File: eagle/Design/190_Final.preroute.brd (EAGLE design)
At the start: 160 x 100 mm, 29 parts, among them U1_0_BRAIN ADAFRUIT-PRO-TRINKET-5V-BOB, U1_6_CASTER CASTERADAFRUIT-3/4IN, U1_7_CASTER_2 CASTERADAFRUIT-3/4IN

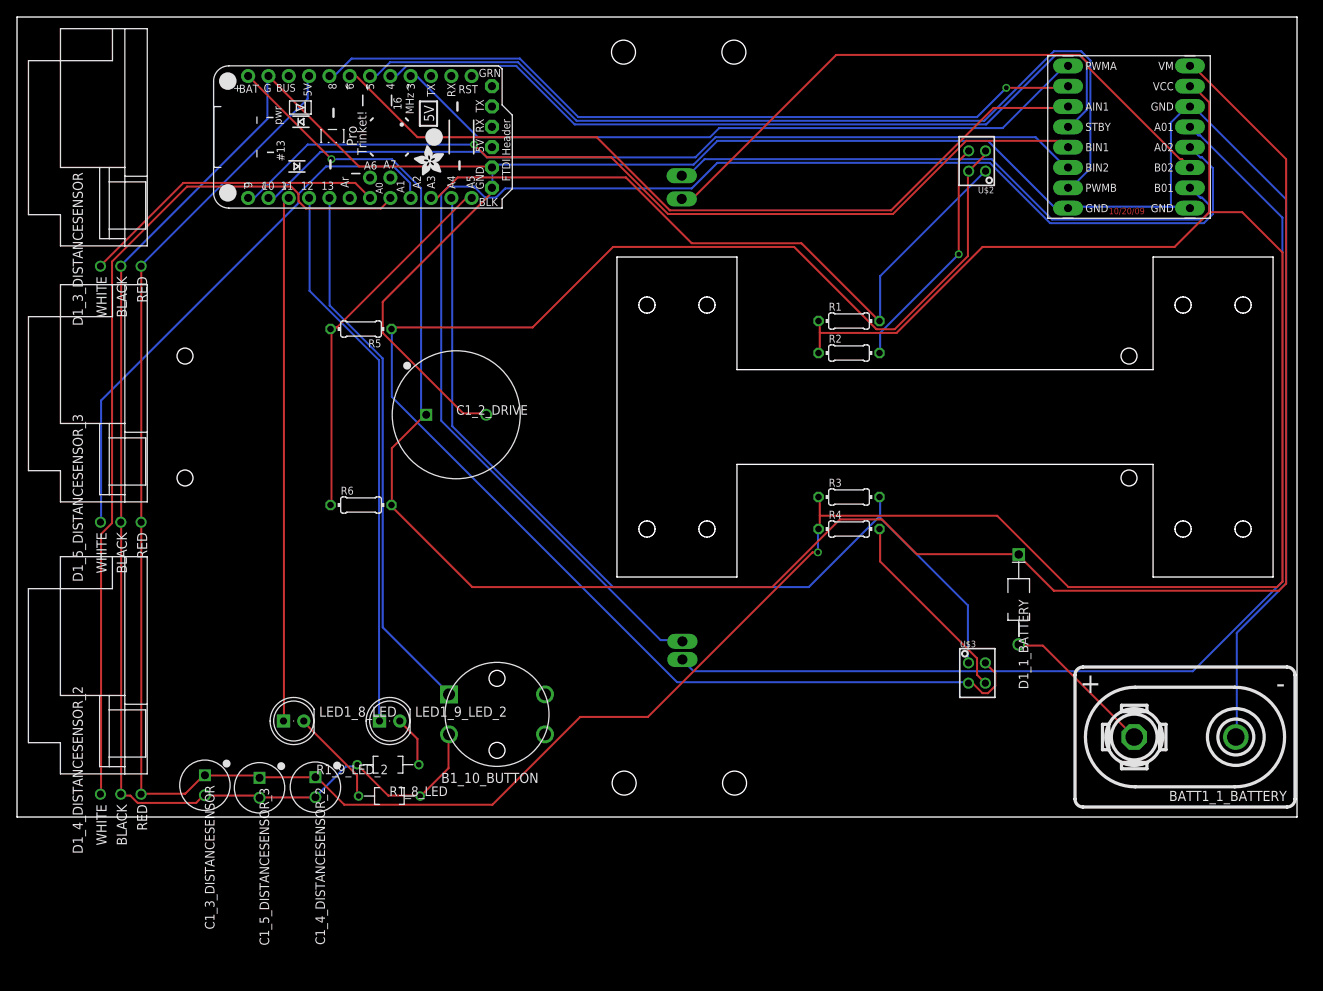
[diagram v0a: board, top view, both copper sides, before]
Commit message: caught a nasty electric bug
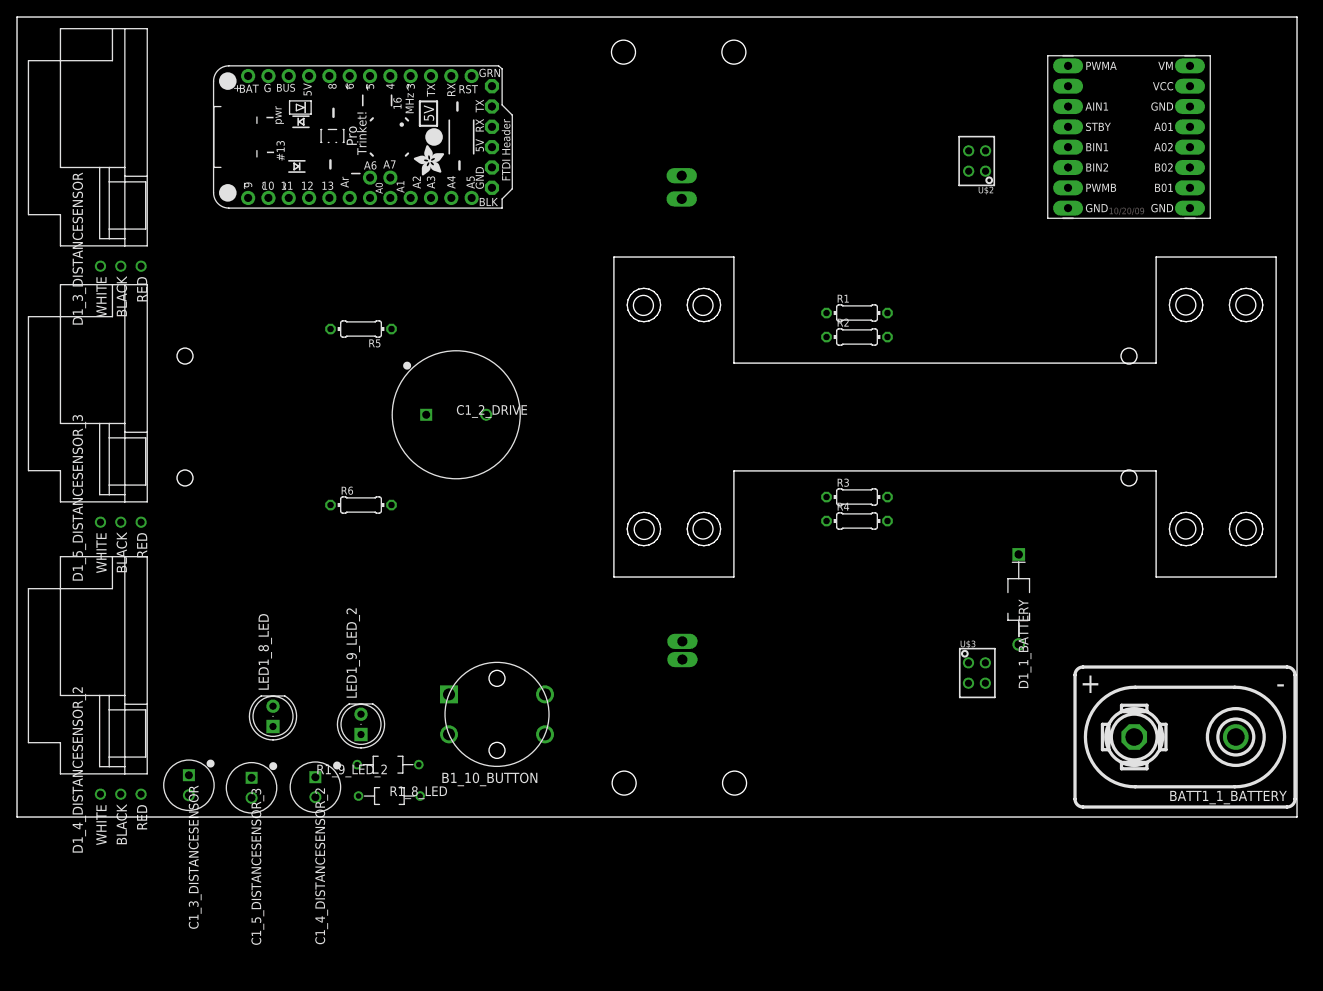
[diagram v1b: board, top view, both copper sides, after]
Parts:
- moved LED1_9_LED_2 3.60 mm to (-37.0, -38.4), turned to 90 degrees
- moved LED1_8_LED 2.64 mm to (-48.0, -37.4), turned to 90 degrees
- moved R2 2.24 mm to (25.0, 10.0)
- moved C1_3_DISTANCESENSOR 2.00 mm to (-58.5, -46.0)
- moved R1 1.41 mm to (25.0, 13.0)
- moved R4 1.41 mm to (25.0, -13.0)
- moved C1_5_DISTANCESENSOR_3 1.00 mm to (-50.7, -46.3)
- moved R3 1.00 mm to (25.0, -10.0)
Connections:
- net GND: no longer U$2.2, U$2.4, U$3.2, U$3.4
- net GND_0_BRAIN: now also U$2.2, U$2.4, U$3.2, U$3.4
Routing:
- net GND_0_BRAIN: track 417.6 -> 0.00 mm
- net +5V_0_BRAIN: track 396.2 -> 0.00 mm, vias 1 -> 0
- net POS_1_BATTERY: track 262.9 -> 0.00 mm, vias 1 -> 0
- net GND: track 201.6 -> 0.00 mm
- net A02_2_DRIVE: track 182.4 -> 0.00 mm
- net A01_2_DRIVE: track 142.0 -> 0.00 mm
- net A4_0_BRAIN: track 119.4 -> 0.00 mm
- net D5_0_BRAIN: track 115.2 -> 0.00 mm
- net D9_0_BRAIN: track 112.9 -> 0.00 mm, vias 1 -> 0
- net A1_0_BRAIN: track 108.1 -> 0.00 mm
- net D10_0_BRAIN: track 105.3 -> 0.00 mm
- net D4_0_BRAIN: track 103.9 -> 0.00 mm
- net D6_0_BRAIN: track 102.2 -> 0.00 mm
- net D8_0_BRAIN: track 97.9 -> 0.00 mm, vias 1 -> 0
- net D3_0_BRAIN: track 89.0 -> 0.00 mm
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
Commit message: more electrical bug catches
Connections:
- removed net GND: R5.1
- net GND_0_BRAIN: now also R5.1
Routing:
- net GND_0_BRAIN: track 0.00 -> 449.8 mm
- net +5V_0_BRAIN: track 0.00 -> 352.4 mm, vias 0 -> 1
- net POS_1_BATTERY: track 0.00 -> 266.5 mm, vias 0 -> 1
- net A02_2_DRIVE: track 0.00 -> 189.1 mm, vias 0 -> 1
- net A01_2_DRIVE: track 0.00 -> 143.0 mm
- net A4_0_BRAIN: track 0.00 -> 137.6 mm
- net D9_0_BRAIN: track 0.00 -> 135.6 mm, vias 0 -> 1
- net D10_0_BRAIN: track 0.00 -> 127.5 mm, vias 0 -> 1
- net A3_0_BRAIN: track 0.00 -> 127.3 mm
- net D5_0_BRAIN: track 0.00 -> 124.0 mm
- net D8_0_BRAIN: track 0.00 -> 117.8 mm, vias 0 -> 1
- net D4_0_BRAIN: track 0.00 -> 111.4 mm
- net D6_0_BRAIN: track 0.00 -> 99.5 mm, vias 0 -> 2
- net D3_0_BRAIN: track 0.00 -> 94.7 mm
- net A1_0_BRAIN: track 0.00 -> 89.6 mm
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
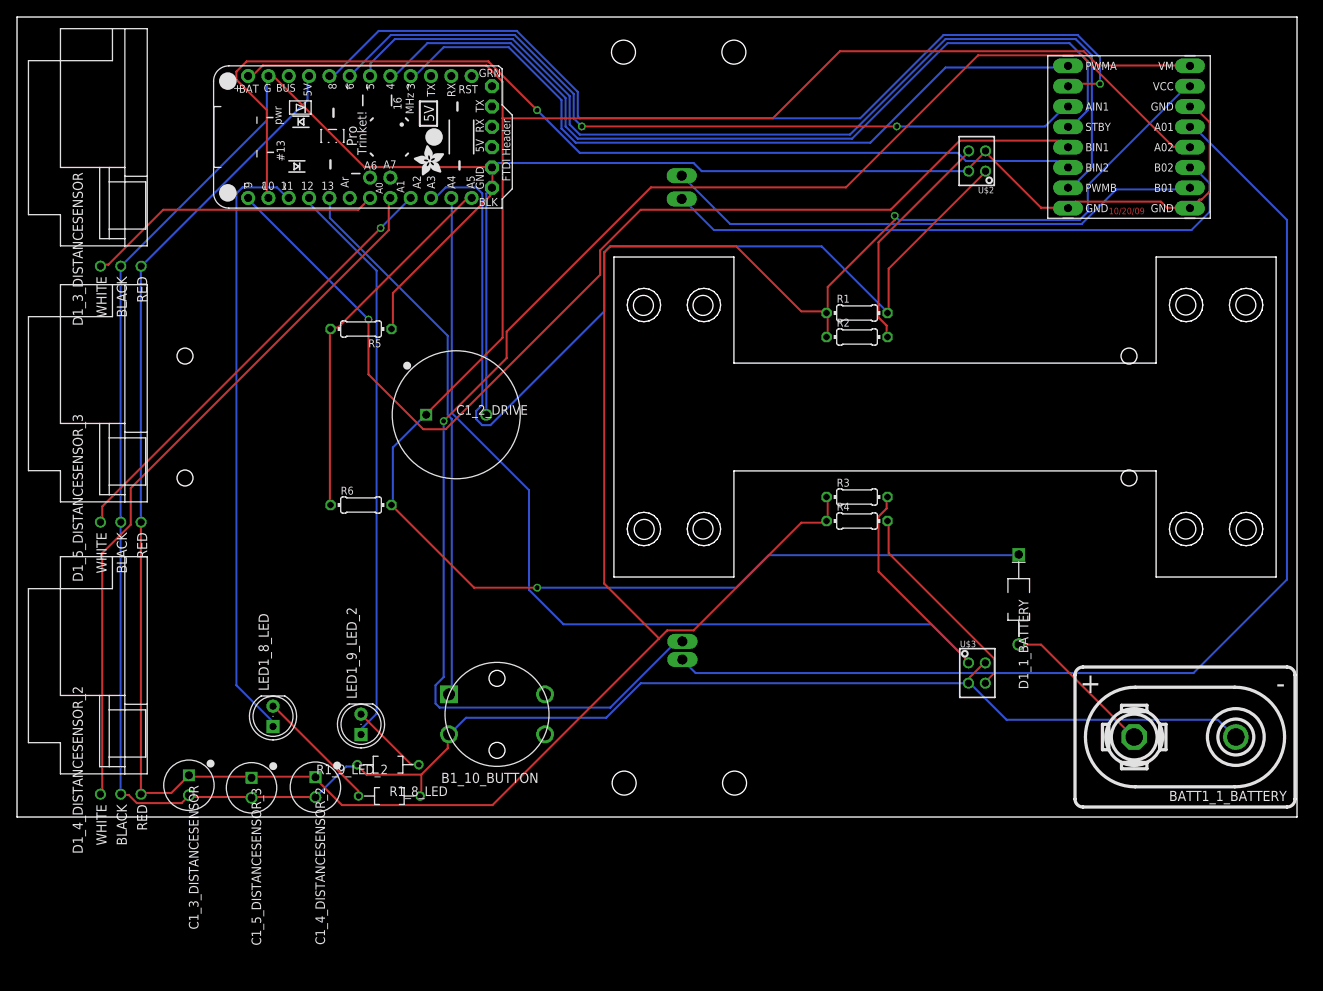
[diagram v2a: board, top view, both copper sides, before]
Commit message: Updated design to use library updates
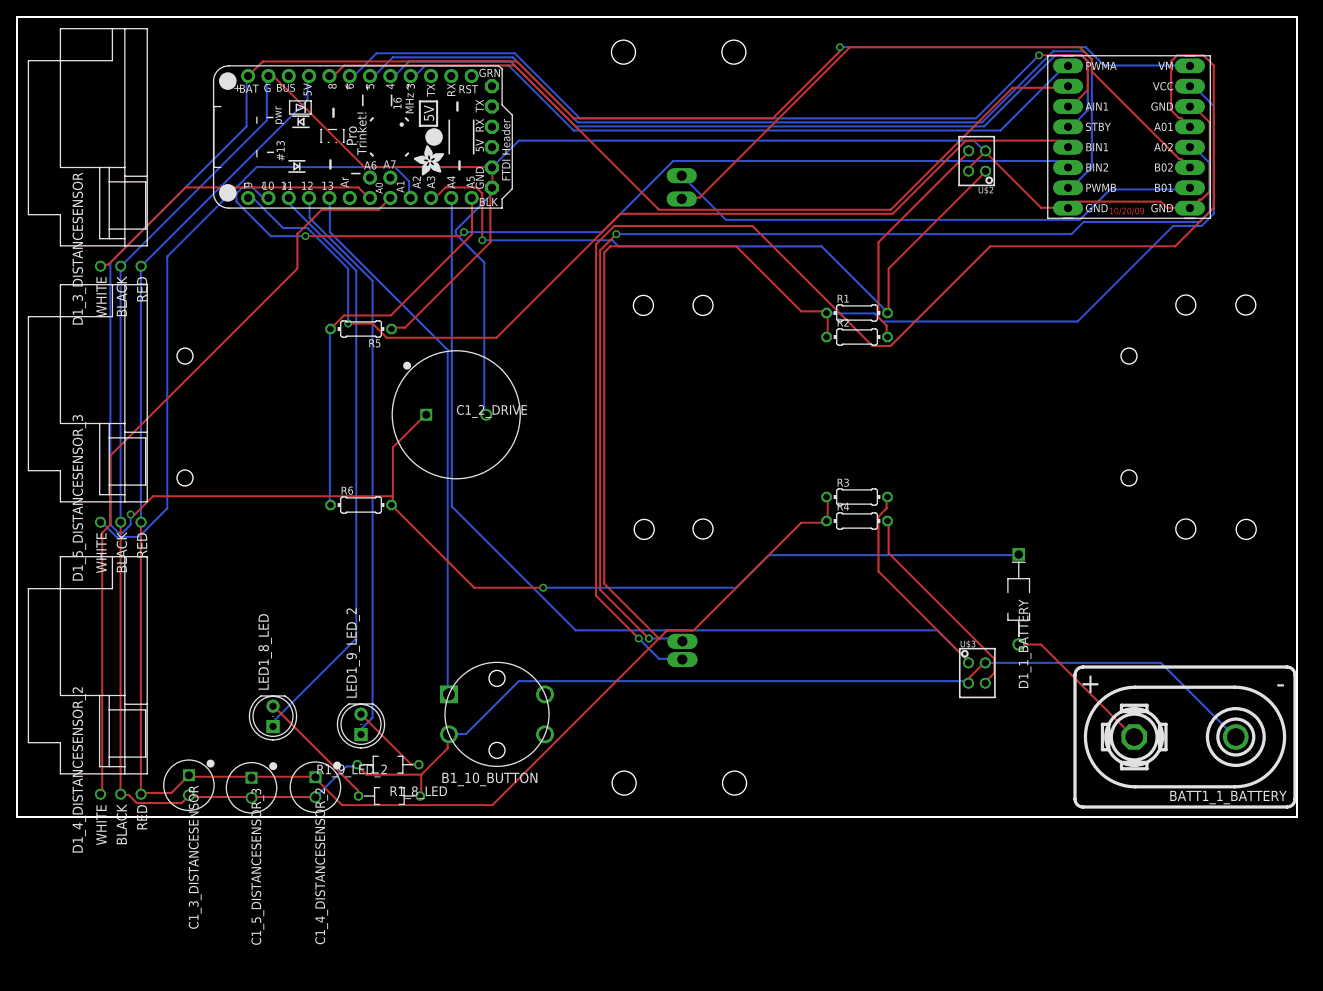
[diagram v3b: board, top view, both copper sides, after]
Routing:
- net POS_1_BATTERY: track 266.5 -> 325.6 mm, vias 1 -> 3
- net A02_2_DRIVE: track 189.1 -> 143.0 mm, vias 1 -> 2
- net A01_2_DRIVE: track 143.0 -> 182.8 mm, vias 0 -> 1
- net A3_0_BRAIN: track 127.3 -> 90.3 mm, vias 0 -> 1
- net A2_0_BRAIN: track 56.6 -> 79.9 mm, vias 1 -> 0
- net D10_0_BRAIN: track 127.5 -> 115.8 mm, vias 1 -> 2
- net D9_0_BRAIN: track 135.6 -> 124.4 mm
- net D8_0_BRAIN: track 117.8 -> 106.8 mm, vias 1 -> 0
- net +5V_0_BRAIN: track 352.4 -> 362.6 mm, vias 1 -> 0
- net D6_0_BRAIN: track 99.5 -> 107.4 mm, vias 2 -> 1
- net D5_0_BRAIN: track 124.0 -> 116.3 mm
- net GND_0_BRAIN: track 449.8 -> 456.5 mm
- net D4_0_BRAIN: track 111.4 -> 104.9 mm
- net D3_0_BRAIN: track 94.7 -> 89.5 mm
- net A1_0_BRAIN: track 89.6 -> 93.7 mm
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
